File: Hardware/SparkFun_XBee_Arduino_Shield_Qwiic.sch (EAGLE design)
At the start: 60 parts, among them J1 USB Female Type C Connector, J3 USB Female Type C Connector, J4 QWIIC_RIGHT_ANGLE, U1 FSUSB30MUX_MSOP10, U2 AP63203, U3 ESD Diode, U4 FT231XS, U5 ESD Diode

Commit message: Routes all airwires, adds most silk labels
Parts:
- removed LOGO1: SFE_LOGO_NAME.1_INCH, SparkFun-Aesthetics:SFE_LOGO_NAME.1_INCH
- added C14: 4.7uF, SparkFun-Capacitors:4.7UF-0603-6.3V-(10%)
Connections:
- net 3.3V: now also C14.1
- net D10/RSSI_PWM: now also B1.A1; no longer B1.*D10
- net D12/SPI_POCI: now also B1.*D11; no longer B1.D12
- net D2/SPI_CLK: now also B1.D13; no longer B1.D2
- net D3/SPI_!CS!: now also B1.*D10; no longer B1.*D3
- net D4/SPI_PICO: now also B1.D12; no longer B1.D4
- net EN: now also B1.*D3; no longer B1.*D11
- net GND: now also C14.2
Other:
- moved on the sheet: B1, C12

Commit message: Adds all silk
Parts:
- J2: device xbee_smart_modem:XBEE_UPDATEXBEE_SMD_SILK -> xbee_smart_modem:XBEE_UPDATEXBEE_SMD
- LOGO3: value QWIIC_LOGO_3MM -> QWIIC_LOGO_4MM; device SparkFun-Aesthetics:QWIIC_LOGO_3MM -> SparkFun-Aesthetics:QWIIC_LOGO_4MM
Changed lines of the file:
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@@
 <part name="ALED" library="SparkFun-Jumpers" deviceset="JUMPER-SMT_2_NC_TRACE" device="_SILK" package3d_urn="urn:adsk.eagle:package:39281/1"/>
 <part name="LOGO2" library="SparkFun-Aesthetics" deviceset="OSHW-LOGO" device="S"/>
-<part name="LOGO3" library="SparkFun-Aesthetics" deviceset="QWIIC_LOGO" device="_3MM" value="QWIIC_LOGO_3MM"/>
+<part name="LOGO3" library="SparkFun-Aesthetics" deviceset="QWIIC_LOGO" device="_4MM" value="QWIIC_LOGO_4MM"/>
 <part name="U2" library="SparkFun-IC-Power" deviceset="AP63203" device="" value="AP63203"/>
 <part name="L1" library="SparkFun-Coils" deviceset="3.9UH" device="" value="3.9UH"/>
@@
 <part name="GND13" library="SparkFun-PowerSymbols" deviceset="GND" device=""/>
 <part name="GND15" library="SparkFun-PowerSymbols" deviceset="GND" device=""/>
-<part name="J2" library="xbee_smart_modem" deviceset="XBEE_UPDATE" device="XBEE_SMD_SILK"/>
+<part name="J2" library="xbee_smart_modem" deviceset="XBEE_UPDATE" device="XBEE_SMD"/>
 <part name="C6" library="SparkFun-Capacitors" deviceset="10NF" device="-0603-50V-10%" value="10nF"/>
 <part name="C7" library="SparkFun-Capacitors" deviceset="10NF" device="-0603-50V-10%" value="10nF"/>

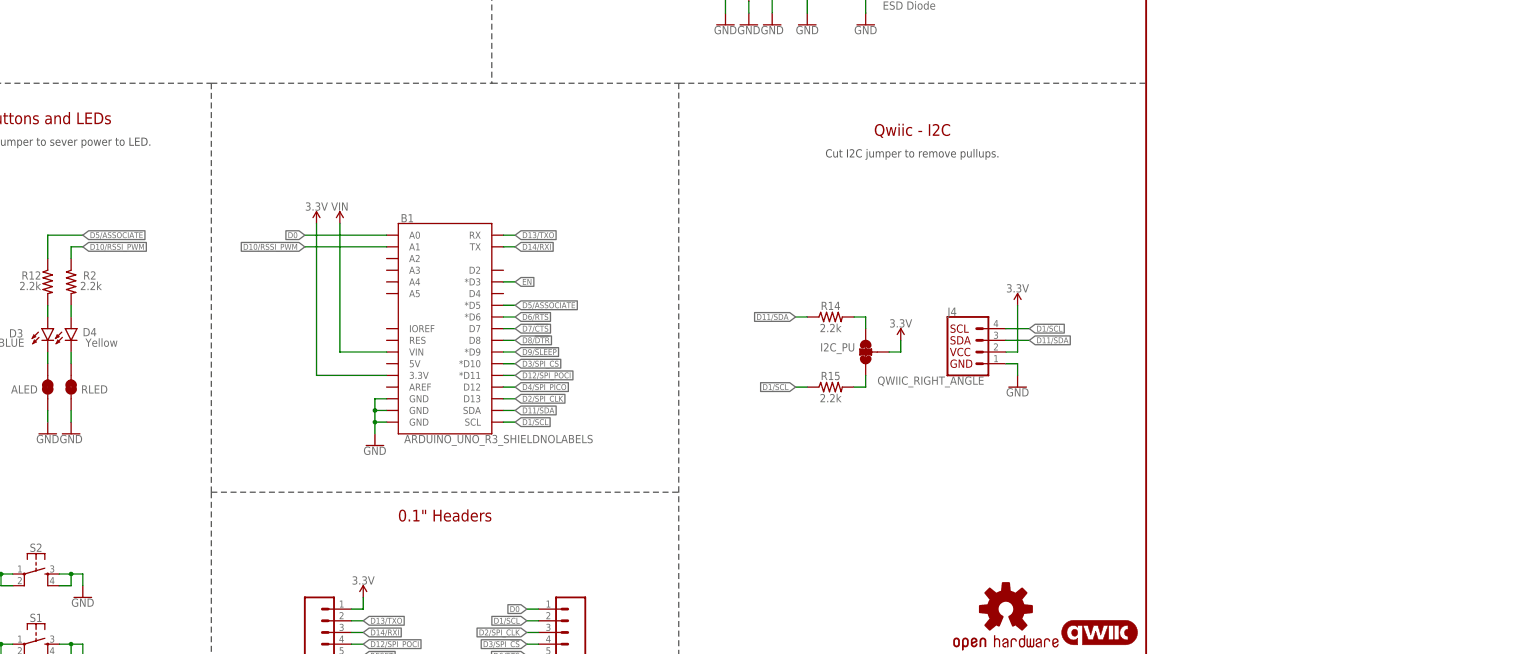
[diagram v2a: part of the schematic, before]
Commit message: Arduino shield now with more level translators!
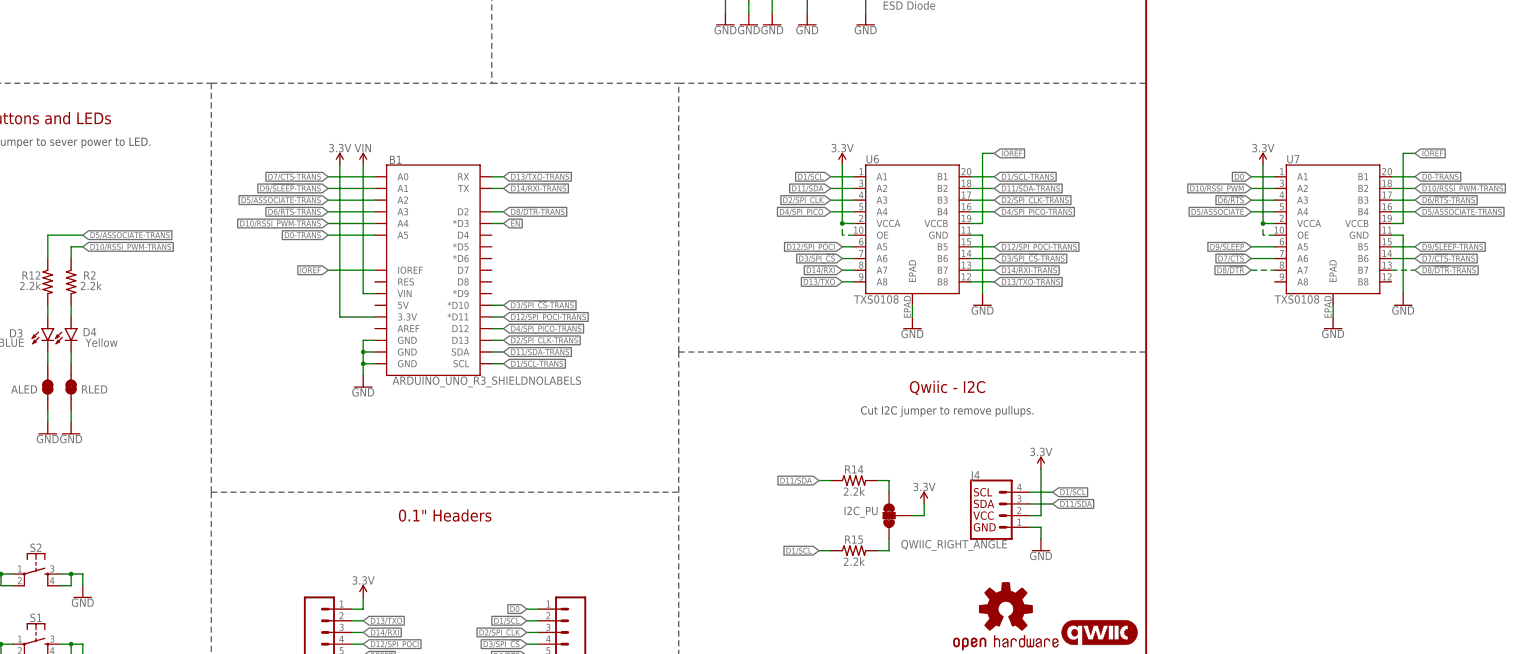
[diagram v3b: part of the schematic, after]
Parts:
- added U6, U7: TXS0108, SparkFun-IC-Comms:TXS0108-VFQFN_20
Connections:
- net FIRMWARE renamed DIRECT_USB
- new net D0-TRANS: B1.A5, U7.B1
- new net D1/SCL-TRANS: B1.SCL, U6.B1
- new net D10/RSSI_PWM-TRANS: B1.A4, R2.1, U7.B2
- new net D11/SDA-TRANS: B1.SDA, U6.B2
- new net D12/SPI_POCI-TRANS: B1.*D11, U6.B5
- new net D13/TXO-TRANS: B1.RX, U6.B8
- new net D14/RXI-TRANS: B1.TX, U6.B7
- new net D2/SPI_CLK-TRANS: B1.D13, U6.B3
- new net D3/SPI_!CS!-TRANS: B1.*D10, U6.B6
- new net D4/SPI_PICO-TRANS: B1.D12, U6.B4
- new net D5/ASSOCIATE-TRANS: B1.A2, R12.1, U7.B4
- new net D6/!RTS!-TRANS: B1.A3, U7.B3
- new net D7/!CTS!-TRANS: B1.A0, U7.B6
- new net D8/!DTR!-TRANS: B1.D2, U7.B7
- new net D9/!SLEEP!-TRANS: B1.A1, U7.B5
- new net IOREF: B1.IOREF, U6.VCCB, U7.VCCB
- net 3.3V: now also U6.OE, U6.VCCA, U7.OE, U7.VCCA
- net D0: now also U7.A1; no longer B1.A0
- net D1/SCL: now also U6.A1; no longer B1.SCL
- net D10/RSSI_PWM: now also U7.A2; no longer B1.A1, R2.1
- net D11/SDA: now also U6.A2; no longer B1.SDA
- net D12/SPI_POCI: now also U6.A5; no longer B1.*D11
- net D13/TXO: now also U6.A8; no longer B1.RX
- net D14/RXI: now also U6.A7; no longer B1.TX
- net D2/SPI_CLK: now also U6.A3; no longer B1.D13
- net D3/SPI_!CS!: now also U6.A6; no longer B1.*D10
- net D4/SPI_PICO: now also U6.A4; no longer B1.D12
- net D5/ASSOCIATE: now also U7.A4; no longer B1.*D5, R12.1
- net D6/!RTS!: now also U7.A3; no longer B1.*D6
- net D7/!CTS!: now also U7.A6; no longer B1.D7
- net D8/!DTR!: now also U7.A7; no longer B1.D8
- net D9/!SLEEP!: now also U7.A5; no longer B1.*D9
- net GND: now also U6.EPAD, U6.GND, U7.EPAD, U7.GND
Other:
- moved on the sheet: B1, I2C_PU, J4, R14, R15

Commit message: Adds silk in relevant places
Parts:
- added JP3: JUMPER-SMT_3_NO_SILK, SparkFun-Jumpers:JUMPER-SMT_3_NO_SILK
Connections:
- new net 5V: B1.5V, JP3.3
- net 3.3V: now also JP3.1
- net EN: now also B1.*D9; no longer B1.*D3
- net IOREF: now also JP3.2
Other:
- note added: "3.3V - > 3.3V - 5V"
- note added: "IOREF Selection"
- note added: "R3 Footprint Plated Through Hole"
- note added: "USE IF THERE IS NO IOREF ON YOUR BASE BOARD"
- note added: "XBee to R3 Footprint Level Translation"
- moved on the sheet: ALED, B1, C11, C12, C13, C14, D2, D3, D4, PLED, R1, R11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

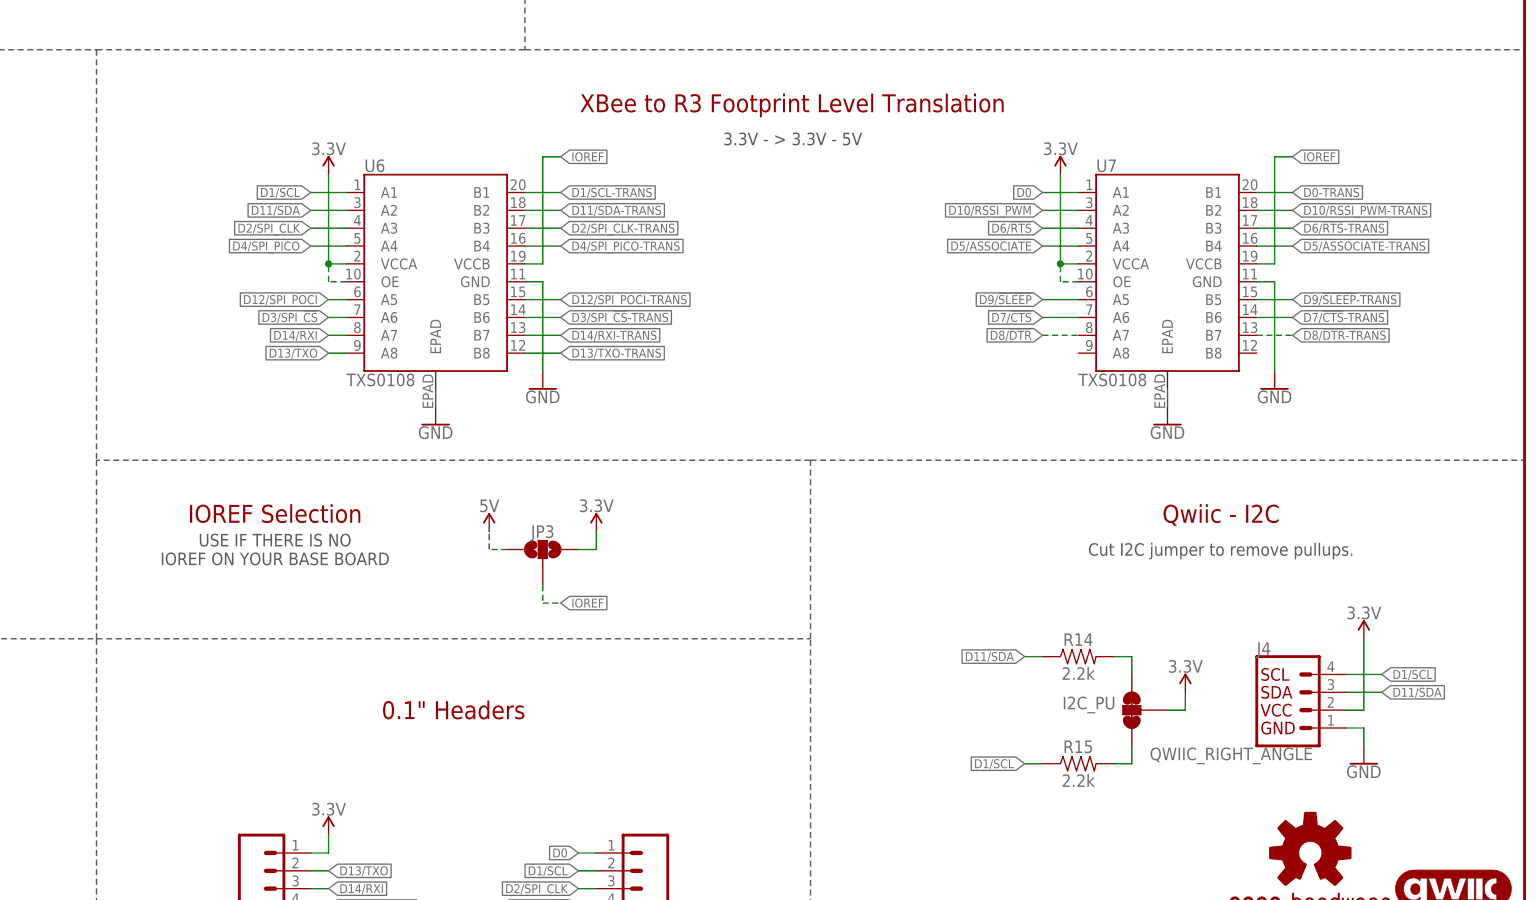
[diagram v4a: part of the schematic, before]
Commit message: Adds decoupling caps to TXS0108E and attempts to fix the silk
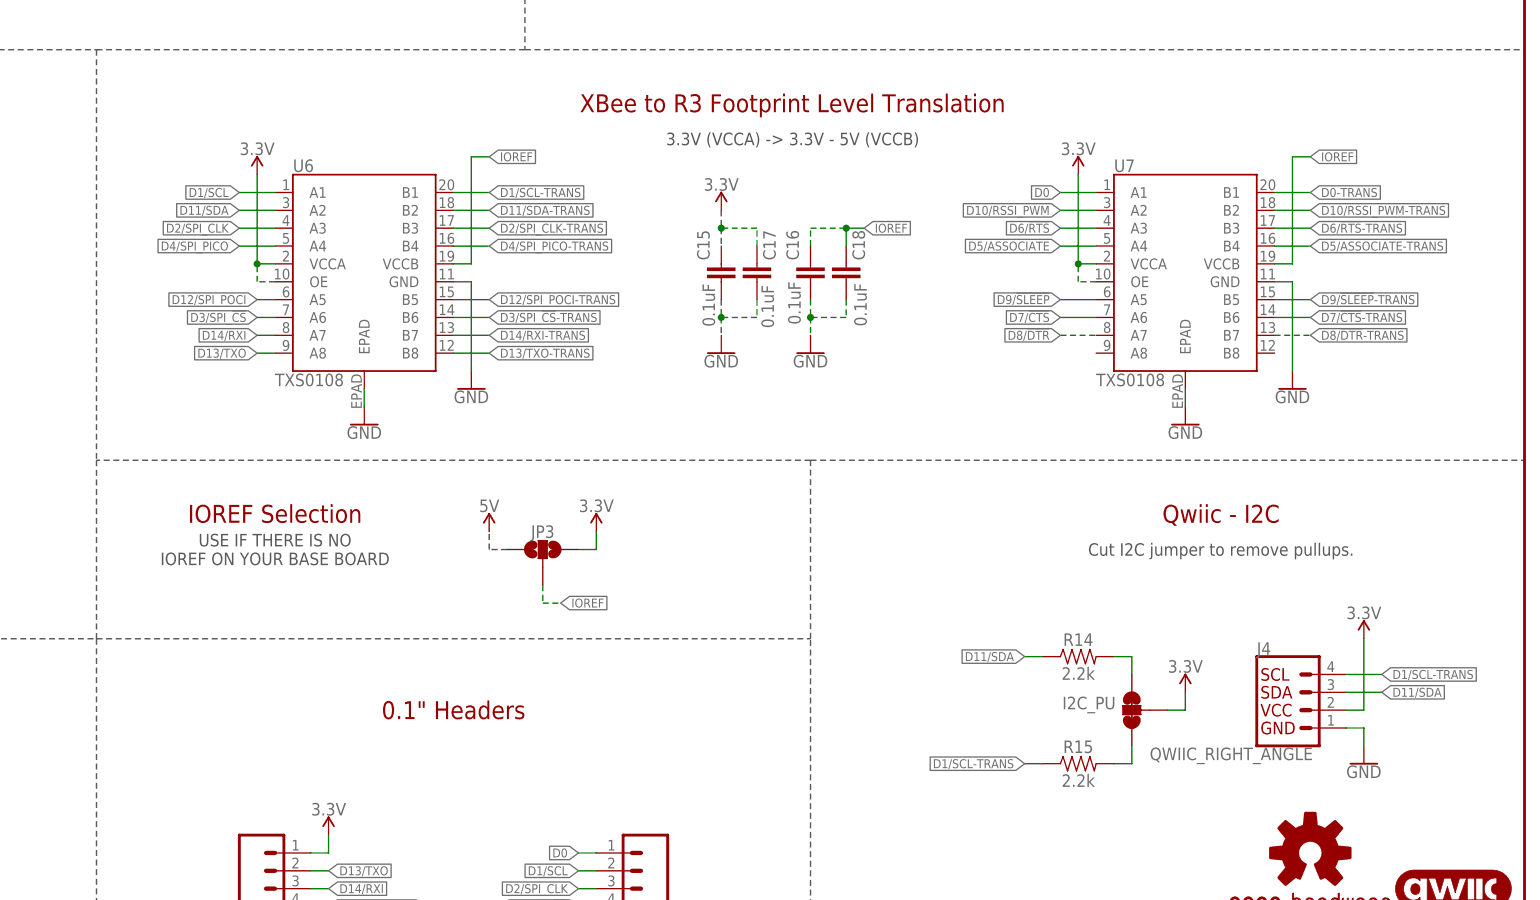
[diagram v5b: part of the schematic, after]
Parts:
- added C15, C16, C17, C18: 0.1uF, SparkFun-Capacitors:0.1UF-0603-25V-(+80/-20%)
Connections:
- net 3.3V: now also C15.1, C17.1
- net D1/SCL: no longer J4.4, R15.1
- net D1/SCL-TRANS: now also J4.4, R15.1
- net GND: now also C15.2, C16.2, C17.2, C18.2
- net IOREF: now also C16.1, C18.1
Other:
- note added: "3.3V (VCCA) -> 3.3V - 5V (VCCB)"
- note removed: "3.3V - > 3.3V - 5V"
- moved on the sheet: U6, U7

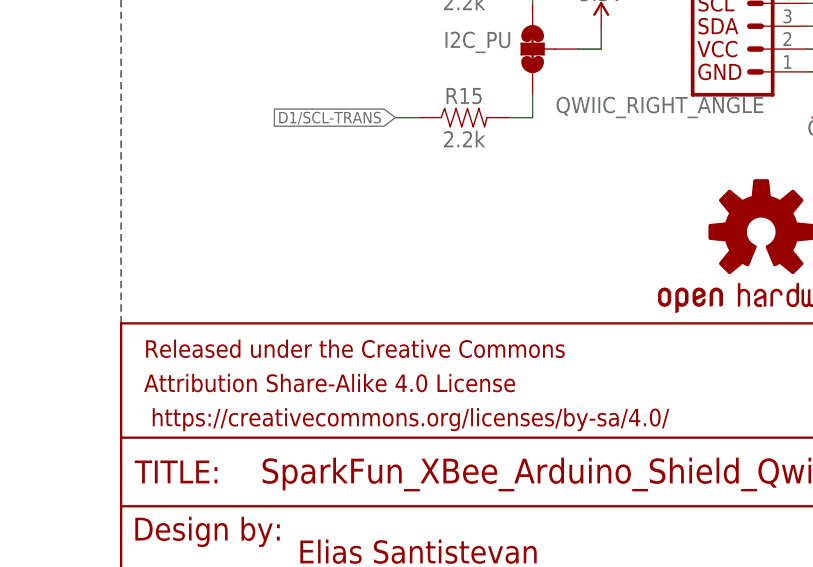
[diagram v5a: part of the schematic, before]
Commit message: Adds a few more labels
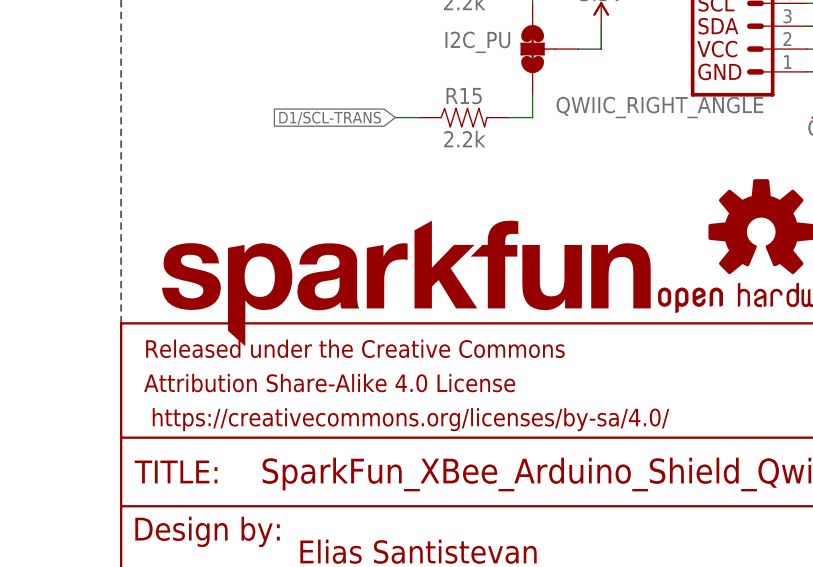
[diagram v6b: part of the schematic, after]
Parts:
- added LOGO1: SFE_LOGO_NAMEBLANK, SparkFun-Aesthetics:SFE_LOGO_NAMEBLANK
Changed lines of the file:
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@@
 <part name="GND34" library="SparkFun-PowerSymbols" deviceset="GND" device=""/>
 <part name="SUPPLY27" library="SparkFun-PowerSymbols" deviceset="3.3V" device=""/>
+<part name="LOGO1" library="SparkFun-Aesthetics" deviceset="SFE_LOGO_NAME" device="BLANK"/>
 </parts>
 <sheets>
@@
 <attribute name="VALUE" x="317.5" y="139.954" size="1.778" layer="96" font="vector" rot="MR0" align="bottom-center"/>
 </instance>
+<instance part="LOGO1" gate="G$1" x="332.74" y="33.02" smashed="yes"/>
 </instances>
 <busses>

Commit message: Fixes a number of silk issues
* Decreases the length delta (haha) between Direct USB data lines
* Adds some clarifying text to the USB connectors
* Adds title to the USB Mux section
* Adjusts a number of traces around for better ground pour
* Moves resistors away from LEDs so that the parts are not so cramped
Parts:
- removed J1, J3: USB Female Type C Connector, SparkFun-Connectors:USB_C_4-LAYER-ISOLATED
- added DIRECT_USB, UART: USB Female Type C Connector, SparkFun-Connectors:USB_C_4-LAYER-ISOLATED
- R3: value 10k -> 100k; device SparkFun-Resistors:10KOHM-0603-1/10W-1% -> SparkFun-Resistors:100KOHM-0603-1/10W-1%
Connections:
- net D+: now also UART.D+; no longer J3.D+
- net D-: now also UART.D-; no longer J3.D-
- net DIRECT_D+: now also DIRECT_USB.D+; no longer J1.D+
- net DIRECT_D-: now also DIRECT_USB.D-; no longer J1.D-
- net GND: now also DIRECT_USB.GND, UART.GND; no longer J1.GND, J3.GND
- net N$14: now also DIRECT_USB.CC2; no longer J1.CC2
- net N$15: now also DIRECT_USB.CC1; no longer J1.CC1
- net N$5: now also UART.CC2; no longer J3.CC2
- net N$6: now also UART.CC1; no longer J3.CC1
- net SHLD: now also UART.SHLD; no longer J3.SHLD
- net SHLD1: now also DIRECT_USB.SHLD; no longer J1.SHLD
- net V_USB: now also UART.VBUS; no longer J3.VBUS
- net V_USB_2: now also DIRECT_USB.VBUS; no longer J1.VBUS
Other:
- note added: "Cut SHLD/SHLD1 jumper to disconnect respective USB Shield from Ground."
- note added: "USB Multiplexer - FSUSB30"
- note added: "Use "Direct USB" USB-C for Cellular Firmware Updates"
- note added: "Use "UART" USB-C for general operation."
- note removed: "Cut SHLD jumper to disconnect USB Shield from Ground."
- moved on the sheet: R13, R16, R7, R8, SHLD, SHLD1, U3, U5
